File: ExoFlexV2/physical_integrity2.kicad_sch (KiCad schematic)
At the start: 35 parts

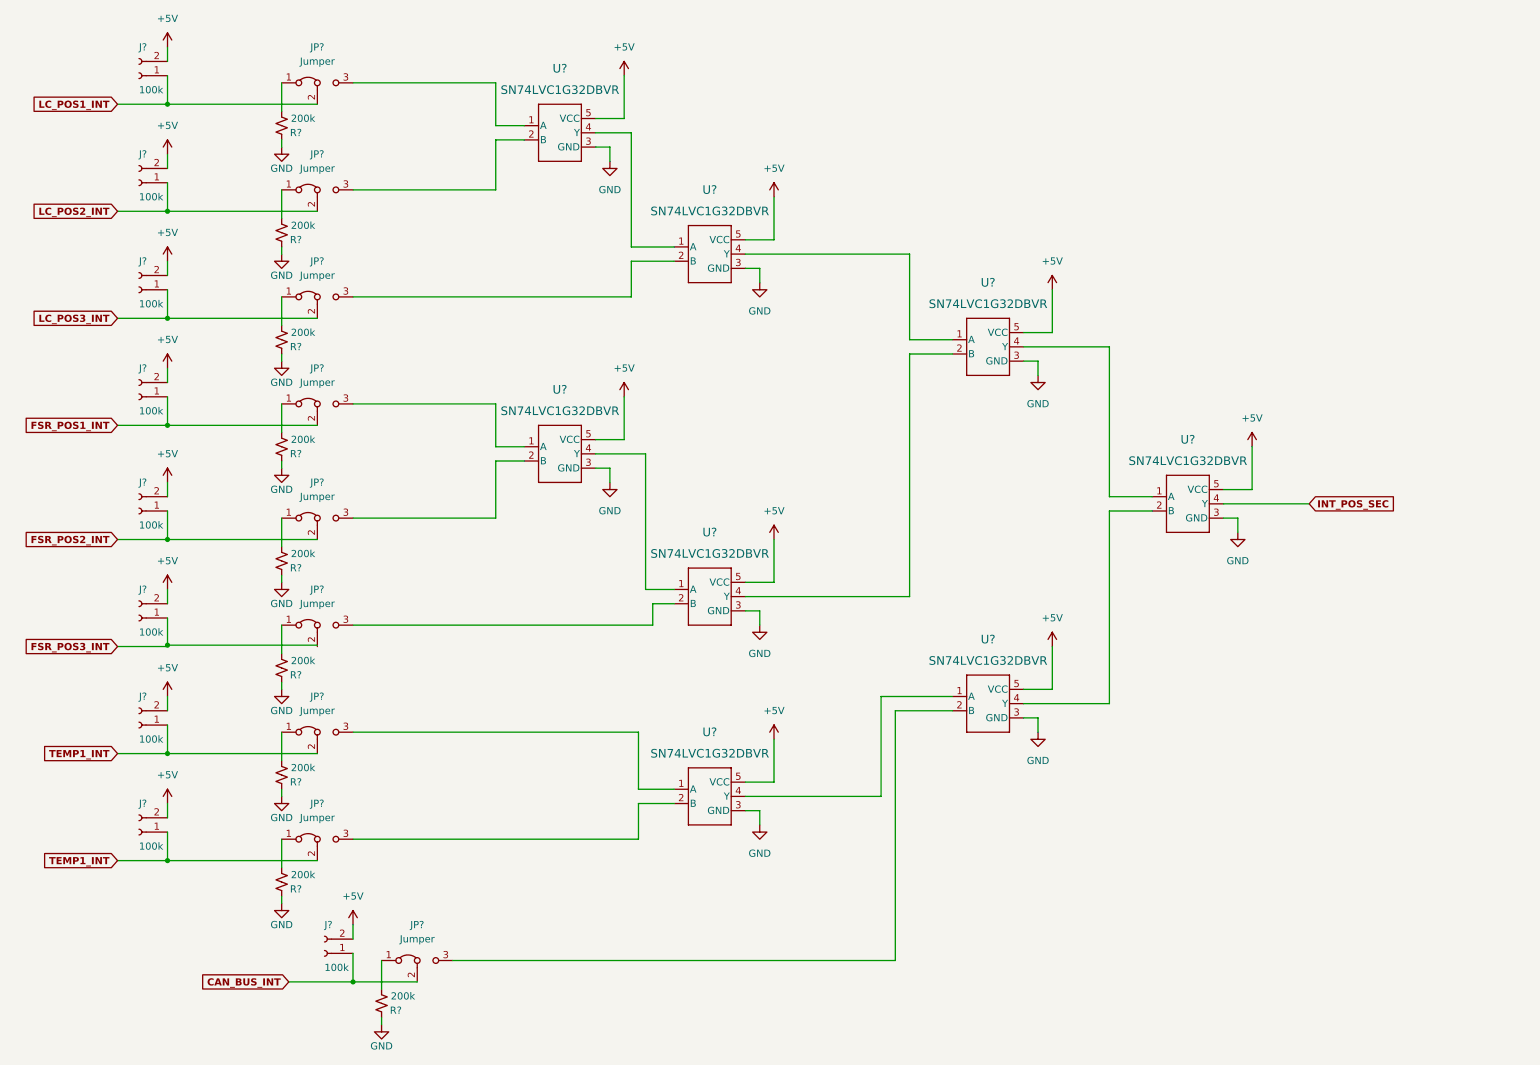
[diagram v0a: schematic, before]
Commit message: Mise à jour signaux STM
- Condo de découplage
- Signaux supplémentaire pour le STM
- Page GND sera pour Multiplexeur
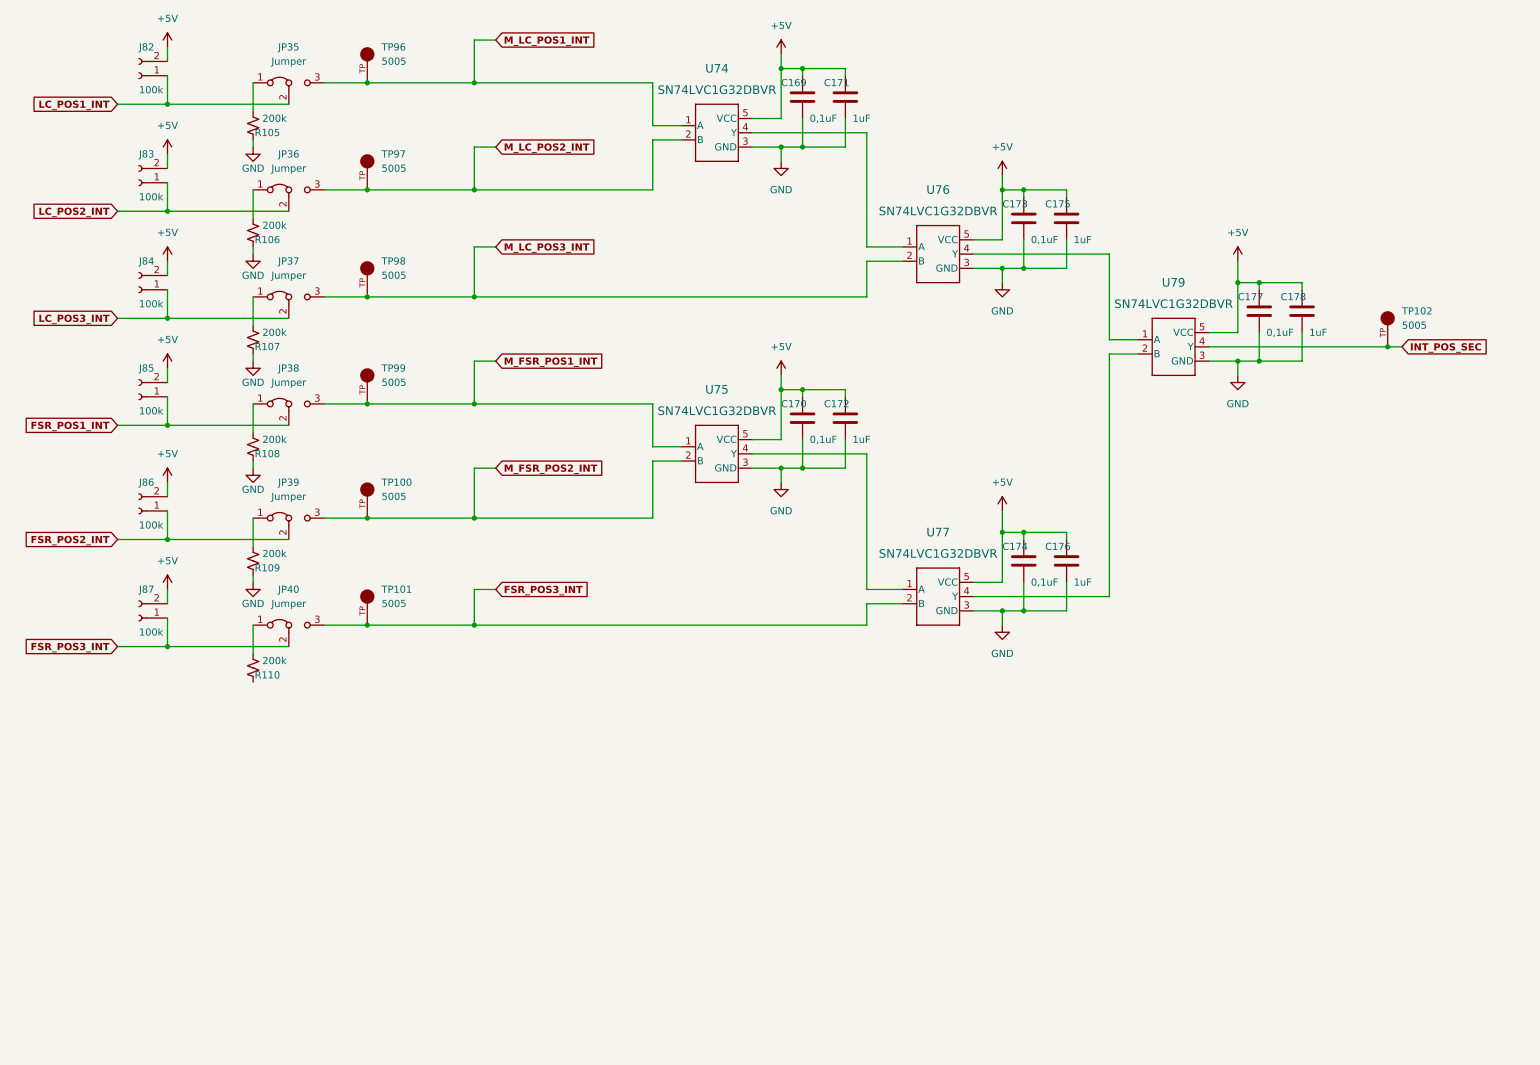
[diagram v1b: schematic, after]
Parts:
- removed J? (x3): 100k, Connector_PinHeader_2.54mm:PinHeader_1x02_P2.54mm_Vertical, symbol Connector:Conn_01x02_Female
- removed JP? (x3): Jumper, Connector_PinHeader_2.54mm:PinHeader_1x03_P2.54mm_Vertical, symbol Jumper:Jumper_3_Bridged12
- removed R? (x3): 200k, Resistor_SMD:R_0603_1608Metric, symbol Device:R_Small_US
- removed U? (x3): SN74LVC1G32DBVR, FootPrint:SOT95P270X145-5N, symbol SymLib:SN74LVC1G32DBVR
- added C169, C170, C173, C174, C177: 0,1uF, Capacitor_SMD:C_0603_1608Metric, symbol Device:C
- added C171, C172, C175, C176, C178: 1uF, Capacitor_SMD:C_0603_1608Metric, symbol Device:C
- added TP100, TP101, TP102, TP96, TP97, TP98, TP99: 5005, FootPrint:KEYSTONE_5005, symbol SymLib:5005
- gave numbers to parts that had none: 23
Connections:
- net +5V: now also C169.1, C170.1, C171.1, C172.1, C173.1, C174.1, C175.1, C176.1, C177.1, C178.1
- net FSR_POS3_INT: now also JP40.2 (C), JP40.3 (B), U77.2 (B), TP101.TP
- net GND: now also C169.2, C170.2, C171.2, C172.2, C173.2, C174.2, C175.2, C176.2, C177.2, C178.2; no longer R110.2
- net INT_POS_SEC: now also U79.4 (Y), TP102.TP
- net M_FSR_POS1_INT: now reaches JP38.3 (B), U75.1 (A)
- net M_FSR_POS1_INT: now also TP99.TP
- net M_LC_POS1_INT: now reaches JP35.3 (B), U74.1 (A)
- net M_LC_POS1_INT: now also TP96.TP
- net M_LC_POS2_INT: now reaches JP36.3 (B), U74.2 (B)
- net M_LC_POS2_INT: now also TP97.TP
- net M_FSR_POS2_INT: now reaches JP39.3 (B), U75.2 (B)
- net M_FSR_POS2_INT: now also TP100.TP
- net M_LC_POS3_INT: now reaches JP37.3 (B), U76.2 (B)
- net M_LC_POS3_INT: now also TP98.TP
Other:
- moved on the sheet: JP35, JP36, JP37, JP38, JP39, JP40, R105, R106, R107, R108, R109, R110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

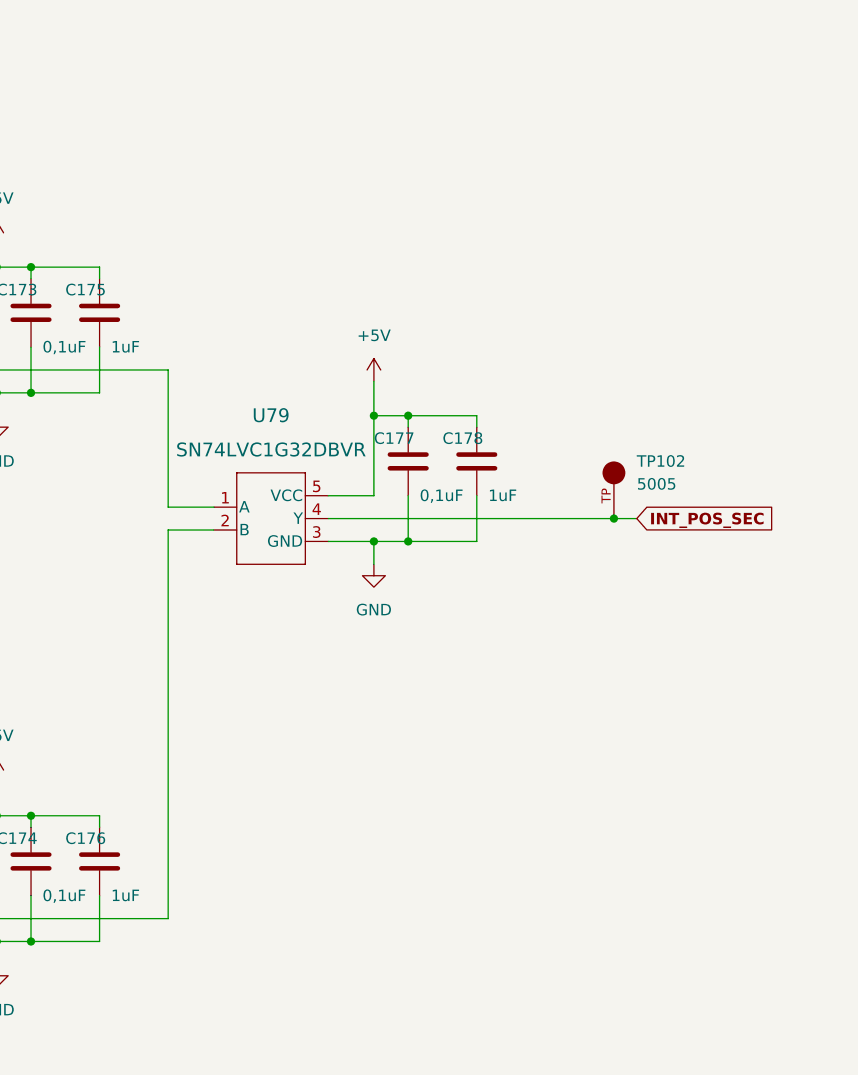
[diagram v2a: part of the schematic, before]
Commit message: Finalisation 1
- Ajout de pages pour la gestion des signaux négatif
- Modification des pages de torque et amplitude
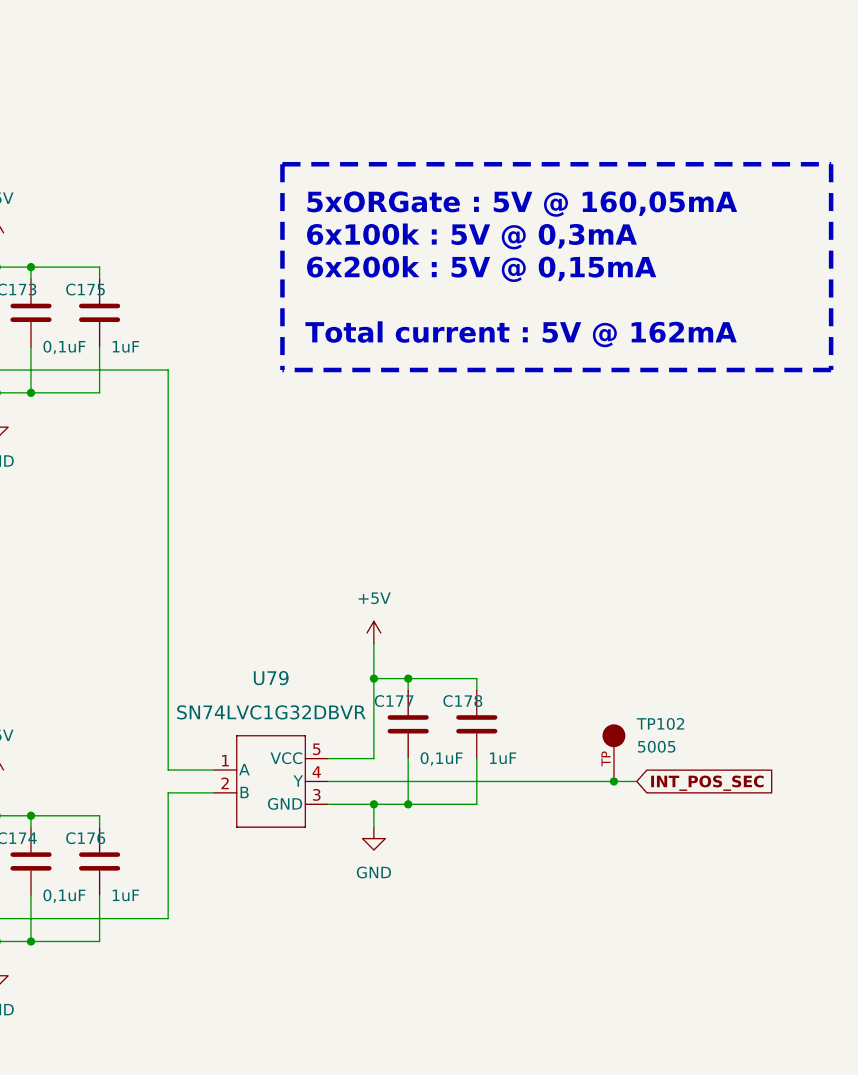
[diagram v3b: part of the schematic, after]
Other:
- note added: "5xORGate : 5V @ 160,05mA 6x100k : 5V @ 0,3mA 6x200k : 5V @ 0,15mA Total current : 5V @ 162mA"
- moved on the sheet: C177, C178, TP102, U79
